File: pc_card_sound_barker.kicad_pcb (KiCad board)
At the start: 2 copper layers, 64.8 x 47.5 mm, 45 parts, among them IC1 MCP100-300D, IC2 74LVC1G00, IC3 MCP100-450D, IC4 TPA152DR, J1 IC1F-68RD-1.27SF(52), J2 G R L, U1 Z8601720ASG, U2 25LCxxx, U3 YMF289B-S, U4 YAC516-E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

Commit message: BOM, tracks, cleanup
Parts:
- IC4: footprint 542MLFT:SOIC127P600X175-8N -> SamacSys_Parts:SOIC127P600X175-8N
- J2: value G R L -> Headphones Out
- JP3: value RW <> RO -> Write Protect
- RN1, RN2: value EXB-D10C104J -> 100k
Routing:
- net AGND: track 175.0 -> 186.4 mm, vias 61 -> 62

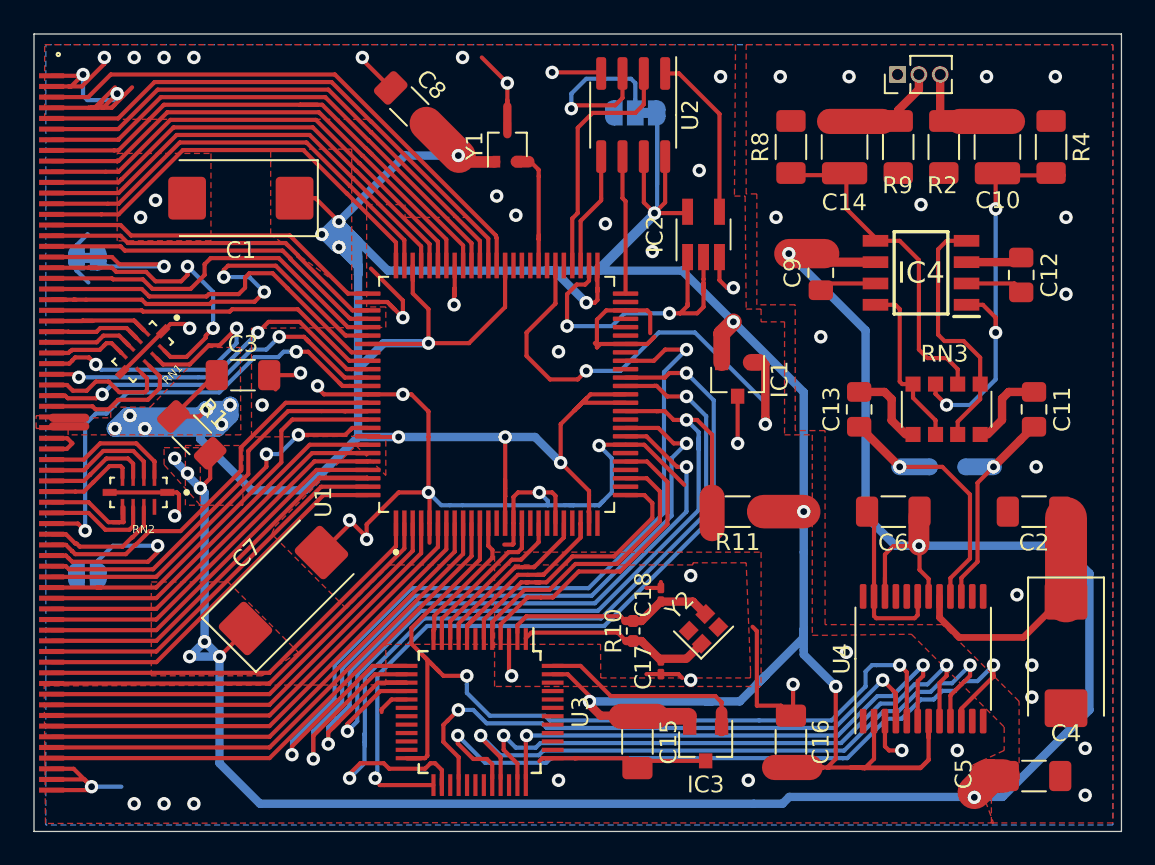
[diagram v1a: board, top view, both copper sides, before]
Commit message: remove pull-downs for unused address lines
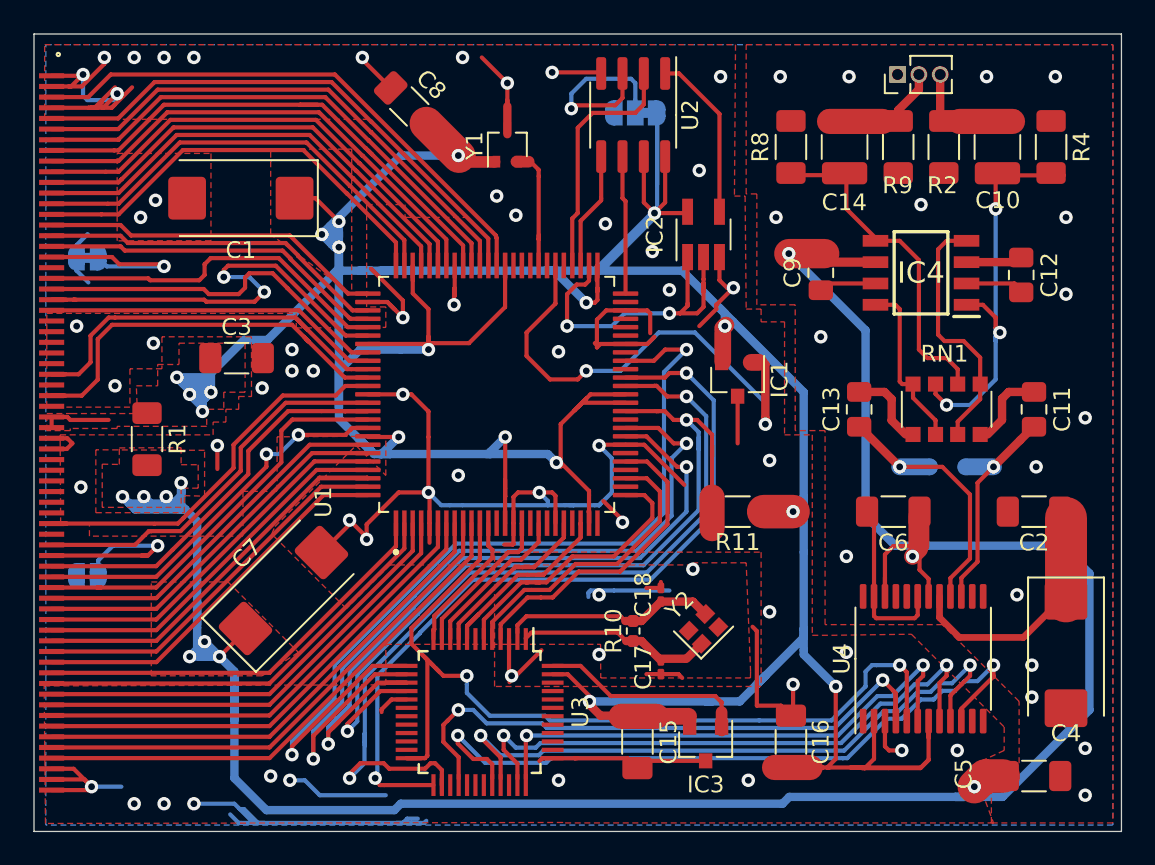
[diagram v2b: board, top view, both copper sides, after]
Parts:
- removed the RN1 at (109.7, 76.2)
- removed RN2: 100k, EXB-D10C104J:RESCAV63P320X160X65-10N
- moved R1 2.68 mm to (110.0, 81.4), turned to 270 degrees
- moved C3 1.09 mm to (115.3, 76.6)
- renumbered RN3 to RN1
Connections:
- J1 pad 10: A11 -> (no net)
- J1 pad 13: A13 -> (no net)
- J1 pad 14: A14 -> (no net)
- J1 pad 19: A16 -> (no net)
- J1 pad 20: A15 -> (no net)
- J1 pad 21: A12 -> (no net)
- J1 pad 46: A17 -> (no net)
- J1 pad 47: A18 -> (no net)
- J1 pad 48: A19 -> (no net)
- J1 pad 49: A20 -> (no net)
- J1 pad 50: A21 -> (no net)
- J1 pad 53: A22 -> (no net)
- J1 pad 54: A23 -> (no net)
- J1 pad 55: A24 -> (no net)
- J1 pad 56: A25 -> (no net)
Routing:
- net AGND: track 186.4 -> 208.5 mm, vias 62 -> 75
- net A19: track 19.1 -> 0.00 mm, vias 2 -> 0
- net A11: track 17.8 -> 0.00 mm, vias 2 -> 0
- net AVDD: track 142.0 -> 158.2 mm, vias 9 -> 10
- net A21: track 8.63 -> 0.00 mm
- net A25: track 8.23 -> 0.00 mm
- net A17: track 8.07 -> 0.00 mm
- net A16: track 7.96 -> 0.00 mm
- net A20: track 7.50 -> 0.00 mm
- net A22: track 7.21 -> 0.00 mm
- net A12: track 6.77 -> 0.00 mm
- net A24: track 6.51 -> 0.00 mm
- net A15: track 6.39 -> 0.00 mm
- net A13: track 5.87 -> 0.00 mm
- net A23: track 5.50 -> 0.00 mm
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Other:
- net class Default: clearance 0.15 -> 0.12
- net class VCC: clearance 0.15 -> 0.12
- rule trace_clearance: 0.15 -> 0.12

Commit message: eeprom is isolated for onboard programming
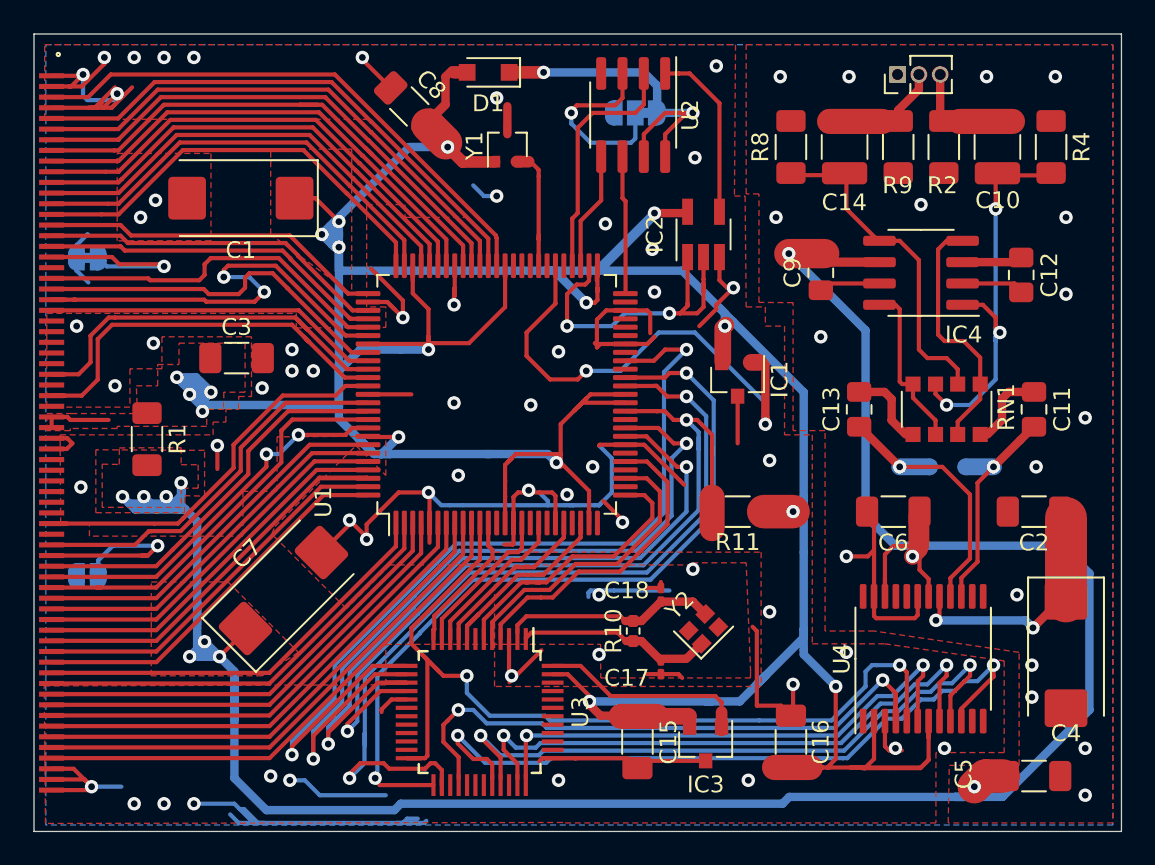
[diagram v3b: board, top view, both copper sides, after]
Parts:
- added D1: Generic 250mA, Diode_SMD:D_SOD-323_HandSoldering, F.Cu at (130.3, 59.6)
- IC1: value MCP100-300D -> SV 3.3V
- IC3: value MCP100-450D -> SV 4.5V
- IC4: footprint SamacSys_Parts:SOIC127P600X175-8N -> Package_SO:SOIC-8_3.9x4.9mm_P1.27mm
- J1: value IC1F-68RD-1.27SF(52) -> PCMCIA Connector
- J2: value Headphones Out -> L R G
- JP3: value Write Protect -> RW RO
- U1: footprint Z8601720ASG:QFP50P1600X1600X160-100N -> Package_QFP:VQFP-100_14x14mm_P0.5mm
- Y1: value MAX7375AXR425 -> 4.19MHz
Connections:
- J1 pad 18: VPP -> (no net)
- J1 pad 52: VPP -> (no net)
- JP3 pad 1: VCC -> VPP
- U2 pad 7: VCC -> VPP
- U2 pad 8: VCC -> VPP
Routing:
- net VCC: track 291.9 -> 270.5 mm, vias 18 -> 17
- net VPP: track 2.74 -> 21.2 mm, vias 0 -> 2
- net AGND: track 208.5 -> 197.6 mm, vias 75 -> 74
- net (no net): track 0.00 -> 2.74 mm
- net VCOM: track 16.3 -> 15.9 mm, vias 0 -> 2
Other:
- board text added: "Card Barker OPL3 Sound Card PCMCIA PC Card Prototype One yottatsa.name/cardbarker"
- board text added: "THIS SIDE UP"
- board text removed: "Card Barker OPL3 Sound Card PCMCIA PC Card Prototype one yottatsa.name/cardbarker"
